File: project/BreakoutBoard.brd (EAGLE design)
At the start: 45.2 x 45.2 mm, 2 parts, among them J1 XF2L-2435-1, X1 LCD

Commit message: Layout complete
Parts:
- added B1: RESET, alps:SKSCLDE010
- added B2: BOOT, alps:SKSCLDE010
- added C1: 22pF/50V, SparkFun-Capacitors:0402-TIGHT
- added C105: 2.2uF/16V, rcl:C0603
- added C106: 4.7uF/16V, rcl:C0603
- added C107: 22pF/50V, rcl:C0402
- added C17: 10uF/16V, rcl:C0603
- added C18: 0.1uF/10V, rcl:C0402
- added C19: 1uF/16V, rcl:C0402
- added C2, C5: 10uF/16V, SparkFun-Capacitors:0603
- added C3, C4: 0.1uF/10V, SparkFun-Capacitors:0402
- added C86: (no value), rcl:C0402
- added CN2: (no value), adafruit:JST-PH-2-SMT
- added D1, D15: (no value), diode:SOD123
- added D10, D8, D9: LESD5D5.0CT1G, discrete:SOD523
- added D11, D12, D2: LESD8D3.3CAT5G, discrete:SOD882
- added D19: (no value), adafruit:SOD-523
- added D3: (no value), led:CHIPLED_1206
- added J2: I2C2, SparkFun-Connectors:JST04_1MM_VERT
- added J3: LCD, ER-CON0.4-24P:OK-24F024-04
- added L1: 2.2μH, SparkFun-Coils:INDUCTOR_4X4MM
- added L6: 10uH_0.8A, discrete:L3012S
- added R1, R13: 10K, rcl:R0402
- added R111, R112: 0, rcl:R0201
- added R12, R123: 0, rcl:R0603
- added R126: 6.6, rcl:R0402
- added R127: 10, rcl:R0402
- added R2: 680K, rcl:R0402
- added R3: 150K, rcl:R0402
- added R74: 51, rcl:R0201
- added TP1, TP2: (no value), SparkFun-Connectors:PAD.03X.03
- added U1: SY8088, discrete:SOT23-5
- added U15: BD60A60NUX, discrete:VSON008X2030
- added U4: ESP32-S3-WROOM-1, espressif:QFN60_ESP32-S3-WROOM-1_EXP
- J1: value XF2L-2435-1 -> I2C1; device con-omron:XF2L-2435-1 -> SparkFun-Connectors:JST04_1MM_VERT
- X1: value LCD -> (none); device ER-CON0.4-24P:OK-24F024-04 -> Adafruit ItsyBitsy nRF52840 Express:MICROBUILDER_4UCONN_20329
- moved X1 21.5 mm to (19.0, 5.00), turned to 0 degrees
- moved J1 18.1 mm to (2.00, 15.5), flipped to the top, turned to 270 degrees
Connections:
- removed net N$10: J1.10, X1.10
- removed net N$11: J1.11, X1.11
- removed net N$12: J1.12, X1.12
- removed net N$13: J1.13, X1.13
- removed net N$14: J1.14, X1.14
- removed net N$15: J1.15, X1.15
- removed net N$16: J1.16, X1.16
- removed net N$17: J1.17, X1.17
- removed net N$18: J1.18, X1.18
- removed net N$19: J1.19, X1.19
- removed net N$20: J1.20, X1.20
- removed net N$21: J1.21, X1.21
- removed net N$22: J1.22, X1.22
- removed net N$23: J1.23, X1.23
- removed net N$24: J1.24, X1.24
- removed net N$3: J1.3, X1.3
- removed net N$5: J1.5, X1.5
- new net ESP_3V3: C17.1, C18.1, D2.C, R12.2, R13.1, U4.2
- new net GND: B1.1, B2.1, C105.2, C106.2, C107.2, C17.2, C18.2, C19.2, C2.2, C3.2, C4.2, C5.2, C86.2, CN2.2, D10.A, D11.A, D12.A, D2.A, D8.A, D9.A, J1.1, J2.1, J3.15, J3.16, J3.3, J3.4, R123.1, R126.1, R3.1, R74.1, TP2.1, U1.2, U15.7, U15.PAD, U4.1, U4.40, U4.41, U4.42, U4.43, U4.44, U4.45, U4.46, U4.47, U4.48, U4.49
- new net GPIO0: B2.3, D12.C, U4.27
- new net GPIO18: J1.4, U4.11
- new net GPIO19: R111.2, U4.13
- new net GPIO20: R112.2, U4.14
- new net GPIO3: J3.21, U4.15
- new net GPIO4: J3.5, U4.4
- new net GPIO40: J2.4, J3.20, U4.33
- new net GPIO41: J2.3, J3.19, U4.34
- new net GPIO45: R127.1, U4.26
- new net GPIO48: J3.10, J3.18, U15.1, U4.25
- new net GPIO5: J3.9, U4.5
- new net GPIO6: J3.8, U4.6
- new net GPIO7: J3.6, U4.7
- new net GPIO8: J1.3, U4.12
- new net LED_A: C105.1, D19.K, J3.23, J3.24, U15.6
- new net LED_DIM: C107.1, R127.2, U15.3
- new net LED_K: J3.1, J3.2, U15.5
- new net MCU_RST: B1.3, C19.1, D11.C, R13.2, U4.3
- new net MCU_VDD: C1.1, C4.1, C5.1, C86.1, D3.A, J1.2, J2.2, J3.11, J3.12, J3.13, J3.14, J3.17, L1.P$2, R12.1, R2.2, TP1.1
- new net USB_5V: C106.1, C2.1, C3.1, D1.C, D15.C, L6.P$1, R1.1, U1.4, U15.2
- new net USB_DN: D9.C, R111.1, X1.D-
- new net USB_DP: D10.C, R112.1, X1.D+
- new net USB_G: R123.2, X1.BASE@1, X1.BASE@2, X1.GND, X1.SPRT@1, X1.SPRT@2, X1.SPRT@3, X1.SPRT@4
- new net USB_VBUS: D1.A, D8.C, X1.VBUS
- net N$1: now also D19.A, L6.P$2, U15.8; no longer J1.1, X1.1
- net N$2: now also D3.C, R74.2; no longer J1.2, X1.2
- net N$4: now also CN2.1, D15.A; no longer J1.4, X1.4
- net N$6: now also R1.2, U1.1; no longer J1.6, X1.6
- net N$7: now also L1.P$1, U1.3; no longer J1.7, X1.7
- net N$8: now also C1.2, R2.1, R3.2, U1.5; no longer J1.8, X1.8
- net N$9: now also R126.2, U15.4; no longer J1.9, X1.9
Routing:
- net MCU_VDD: track 0.00 -> 84.3 mm, vias 0 -> 2
- net GPIO48: track 0.00 -> 56.4 mm, vias 0 -> 2
- net USB_5V: track 0.00 -> 48.7 mm, vias 0 -> 3
- net GPIO40: track 0.00 -> 41.8 mm, vias 0 -> 4
- net GPIO41: track 0.00 -> 40.5 mm, vias 0 -> 3
- net GND: track 0.00 -> 37.8 mm, vias 0 -> 56
- net N$18: track 31.3 -> 0.00 mm, vias 1 -> 0
- net N$17: track 30.8 -> 0.00 mm, vias 1 -> 0
- net N$19: track 30.5 -> 0.00 mm, vias 1 -> 0
- net N$16: track 30.4 -> 0.00 mm, vias 1 -> 0
- net N$20: track 30.1 -> 0.00 mm, vias 1 -> 0
- net N$15: track 30.0 -> 0.00 mm, vias 1 -> 0
- net N$21: track 29.6 -> 0.00 mm, vias 1 -> 0
- net N$14: track 29.6 -> 0.00 mm, vias 1 -> 0
- net N$22: track 29.2 -> 0.00 mm, vias 1 -> 0
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- added copper zone on layer 1, net GND
- added copper zone on layer 16, net GND
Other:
- board size 45.2 x 45.2 mm -> 38 x 38 mm

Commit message: Layout optimization
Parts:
- removed C107: 22pF/50V, rcl:C0402
- removed CN2: (no value), adafruit:JST-PH-2-SMT
- removed R127: 10, rcl:R0402
- removed TP2: (no value), SparkFun-Connectors:PAD.03X.03
- removed X1: (no value), Adafruit ItsyBitsy nRF52840 Express:MICROBUILDER_4UCONN_20329
- added C97: 0.1uF/6.3V, rcl:C0402
- added C98: 4.7uF/6.3V, rcl:C0402
- added J4: I2C1, SparkFun-Connectors:JST04_1MM_VERT
- added J5: I2C2, SparkFun-Connectors:JST04_1MM_VERT
- added U$1, U$2, U$4, U$5: FIDUCIAL, adafruit:FIDUCIAL_1MM
- C1: device SparkFun-Capacitors:0402-TIGHT -> rcl:C0402
- C2: device SparkFun-Capacitors:0603 -> rcl:C0603
- C3: device SparkFun-Capacitors:0402 -> rcl:C0603
- C4: device SparkFun-Capacitors:0402 -> rcl:C0402
- C5: device SparkFun-Capacitors:0603 -> rcl:C0402
- C86: value (none) -> 0.1uF/6.3V
- J1: value I2C1 -> (none); device SparkFun-Connectors:JST04_1MM_VERT -> Adafruit ItsyBitsy nRF52840 Express:MICROBUILDER_4UCONN_20329
- J2: value I2C2 -> (none); device SparkFun-Connectors:JST04_1MM_VERT -> adafruit:JST-PH-2-SMT
- R126: value 6.6 -> 20K
- TP1: value (none) -> TPTP06R; device SparkFun-Connectors:PAD.03X.03 -> testpad:TP06R
- moved J2 31.2 mm to (33.0, 19.0), turned to 90 degrees
- moved TP1 22.0 mm to (30.6, 30.7)
- moved J1 20.0 mm to (19.0, 5.00), turned to 0 degrees
- moved R2 8.55 mm to (19.5, 9.60), turned to 180 degrees
- moved C1 8.50 mm to (19.5, 10.5), flipped to the bottom, turned to 0 degrees
- moved D12 6.93 mm to (33.4, 9.40)
- moved R3 5.56 mm to (19.5, 8.60), turned to 0 degrees
- moved R74 4.10 mm to (9.39, 9.15), turned to 180 degrees
- moved R126 3.49 mm to (29.2, 30.6), flipped to the bottom
- moved D19 2.24 mm to (33.0, 28.0), turned to 0 degrees
- moved L6 2.00 mm to (33.0, 25.0), flipped to the bottom, turned to 270 degrees
- moved C105 1.77 mm to (30.5, 30.5), turned to 270 degrees
- moved C4 1.70 mm to (29.2, 11.0), turned to 45 degrees
- moved C5 1.31 mm to (30.5, 10.2), turned to 45 degrees
- moved D2 1.30 mm to (7.90, 31.0)
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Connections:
- removed net LED_DIM: C107.1, R127.2, U15.3
- net GND: now also B1.2, B2.2, C97.2, C98.2, J2.2, J4.1, J5.1; no longer C107.2, CN2.2, J1.1, J2.1, TP2.1
- net GPIO0: now also B2.4
- net GPIO18: now also J4.4; no longer J1.4
- net GPIO40: now also J5.4; no longer J2.4
- net GPIO41: now also J5.3; no longer J2.3
- net GPIO45: now also U15.3; no longer R127.1
- net GPIO8: now also J4.3; no longer J1.3
- net LED_K: now also TP1.TP
- net MCU_RST: now also B1.4
- net MCU_VDD: now also C97.1, C98.1, J4.2, J5.2, U15.2; no longer J1.2, J2.2, TP1.1
- net N$4: now also J2.1; no longer CN2.1
- net USB_5V: no longer U15.2
- net USB_DN: now also J1.D-; no longer X1.D-
- net USB_DP: now also J1.D+; no longer X1.D+
- net USB_G: now also J1.BASE@1, J1.BASE@2, J1.GND, J1.SPRT@1, J1.SPRT@2, J1.SPRT@3, J1.SPRT@4; no longer X1.BASE@1, X1.BASE@2, X1.GND, X1.SPRT@1, X1.SPRT@2, X1.SPRT@3, X1.SPRT@4
- net USB_VBUS: now also J1.VBUS; no longer X1.VBUS
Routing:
- net GPIO48: track 56.4 -> 37.1 mm
- net MCU_VDD: track 84.3 -> 99.7 mm, vias 2 -> 5
- net GPIO0: track 20.9 -> 11.6 mm
- net N$8: track 12.4 -> 4.06 mm, vias 2 -> 1
- net GND: track 37.8 -> 46.1 mm, vias 56 -> 60
- net GPIO45: track 14.7 -> 21.5 mm, vias 0 -> 1
- net LED_DIM: track 4.68 -> 0.00 mm, vias 1 -> 0
- net LED_A: track 14.5 -> 17.7 mm, vias 1 -> 2
- net USB_5V: track 48.7 -> 45.6 mm
- net GPIO7: track 14.1 -> 11.1 mm
- net LED_K: track 12.9 -> 15.7 mm
- net N$6: track 2.24 -> 4.63 mm, vias 1 -> 0
- net GPIO6: track 12.3 -> 9.94 mm
- net GPIO5: track 10.7 -> 8.81 mm
- net N$1: track 3.79 -> 5.25 mm
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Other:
- board text added: "5V"
- board text added: "BOOT"
- board text added: "I2C"
- board text added: "RST"

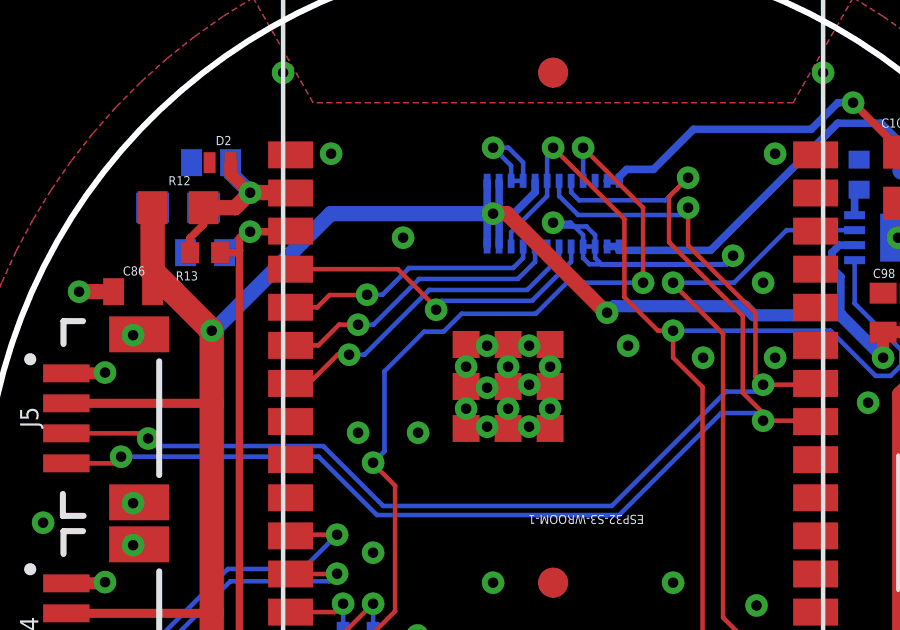
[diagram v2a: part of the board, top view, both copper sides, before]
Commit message: Display pinout fix
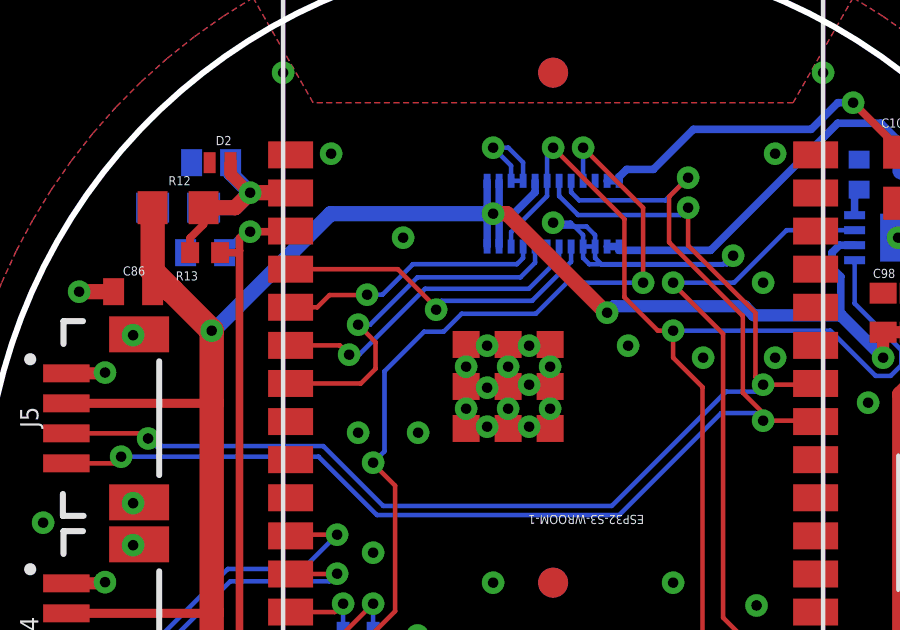
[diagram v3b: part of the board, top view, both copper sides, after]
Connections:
- net GPIO6: now also J3.6; no longer J3.8
- net GPIO7: now also J3.8; no longer J3.6
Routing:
- net GPIO7: track 11.1 -> 12.0 mm
- net GPIO6: track 9.94 -> 10.8 mm
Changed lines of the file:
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@@
 <drawing>
 <settings>
-<setting alwaysvectorfont="no"/>
+<setting alwaysvectorfont="yes"/>
 <setting verticaltext="up"/>
 </settings>
-<grid distance="1" unitdist="mm" unit="mm" style="lines" multiple="1" display="no" altdistance="0.1" altunitdist="mm" altunit="mm"/>
+<grid distance="50" unitdist="mil" unit="mil" style="lines" multiple="1" display="no" altdistance="5" altunitdist="mil" altunit="mil"/>
 <layers>
 <layer number="1" name="Top" color="4" fill="1" visible="yes" active="yes"/>
@@
 <wire x1="12.7878" y1="26.5878" x2="12.8" y2="26.6" width="0.1524" layer="1"/>
 <wire x1="18" y1="28.205" x2="18" y2="27.824" width="0.1524" layer="16"/>
-<wire x1="18" y1="27.824" x2="17.665" y2="27.489" width="0.1524" layer="16"/>
-<wire x1="17.665" y1="27.489" x2="14.197" y2="27.489" width="0.1524" layer="16"/>
-<wire x1="14.197" y1="27.489" x2="13.308" y2="26.6" width="0.1524" layer="16"/>
+<wire x1="18" y1="27.824" x2="17.792" y2="27.616" width="0.1524" layer="16"/>
+<wire x1="17.792" y1="27.616" x2="14.324" y2="27.616" width="0.1524" layer="16"/>
+<wire x1="14.324" y1="27.616" x2="13.308" y2="26.6" width="0.1524" layer="16"/>
 <wire x1="13.308" y1="26.6" x2="12.8" y2="26.6" width="0.1524" layer="16"/>
 </signal>
 <signal name="GPIO6">
 <contactref element="U4" pad="6"/>
-<via x="12.5" y="25.6" extent="1-16" drill="0.35"/>
-<wire x1="10.25" y1="24.91" x2="10.34" y2="25" width="0.1524" layer="1"/>
-<contactref element="J3" pad="8"/>
-<wire x1="10.25" y1="24.91" x2="11.175" y2="24.91" width="0.1524" layer="1"/>
-<wire x1="11.865" y1="25.6" x2="12.5" y2="25.6" width="0.1524" layer="1"/>
-<wire x1="11.865" y1="25.6" x2="11.175" y2="24.91" width="0.1524" layer="1"/>
-<wire x1="18.4" y1="28.205" x2="18.4" y2="27.697" width="0.1524" layer="16"/>
-<wire x1="18.4" y1="27.697" x2="17.827" y2="27.124" width="0.1524" layer="16"/>
-<wire x1="17.827" y1="27.124" x2="14.532" y2="27.124" width="0.1524" layer="16"/>
-<wire x1="14.532" y1="27.124" x2="13.008" y2="25.6" width="0.1524" layer="16"/>
-<wire x1="13.008" y1="25.6" x2="12.5" y2="25.6" width="0.1524" layer="16"/>
+<via x="12.2" y="24.6" extent="1-16" drill="0.35"/>
+<contactref element="J3" pad="6"/>
+<wire x1="12.2" y1="24.6" x2="12.535" y2="24.6" width="0.1524" layer="16"/>
+<wire x1="18.1922875" y1="26.797" x2="19.2" y2="27.8047125" width="0.1524" layer="16"/>
+<wire x1="19.2" y1="27.8047125" x2="19.2" y2="28.205" width="0.1524" layer="16"/>
+<wire x1="12.535" y1="24.6" x2="14.732" y2="26.797" width="0.1524" layer="16"/>
+<wire x1="14.732" y1="26.797" x2="18.1922875" y2="26.797" width="0.1524" layer="16"/>
+<wire x1="12.2" y1="24.6" x2="11.89" y2="24.91" width="0.1524" layer="1"/>
+<wire x1="11.89" y1="24.91" x2="10.25" y2="24.91" width="0.1524" layer="1"/>
 </signal>
 <signal name="GPIO7">
 <contactref element="U4" pad="7"/>
-<via x="12.2" y="24.6" extent="1-16" drill="0.35"/>
-<contactref element="J3" pad="6"/>
-<wire x1="10.25" y1="23.64" x2="10.859" y2="23.64" width="0.1524" layer="1"/>
-<wire x1="11.819" y1="24.6" x2="12.2" y2="24.6" width="0.1524" layer="1"/>
-<wire x1="11.819" y1="24.6" x2="10.859" y2="23.64" width="0.1524" layer="1"/>
-<wire x1="18.135" y1="26.759" x2="14.867" y2="26.759" width="0.1524" layer="16"/>
-<wire x1="14.867" y1="26.759" x2="12.708" y2="24.6" width="0.1524" layer="16"/>
-<wire x1="12.708" y1="24.6" x2="12.2" y2="24.6" width="0.1524" layer="16"/>
-<wire x1="19.2" y1="28.205" x2="19.2" y2="27.824" width="0.1524" layer="16"/>
-<wire x1="19.2" y1="27.824" x2="18.135" y2="26.759" width="0.1524" layer="16"/>
+<via x="12.5" y="25.6" extent="1-16" drill="0.35"/>
+<contactref element="J3" pad="8"/>
+<wire x1="10.25" y1="23.64" x2="12.591" y2="23.64" width="0.1524" layer="1"/>
+<wire x1="13.081" y1="24.13" x2="13.081" y2="25.019" width="0.1524" layer="1"/>
+<wire x1="13.081" y1="25.019" x2="12.5" y2="25.6" width="0.1524" layer="1"/>
+<wire x1="12.591" y1="23.64" x2="13.081" y2="24.13" width="0.1524" layer="1"/>
+<wire x1="12.5" y1="25.6" x2="12.9" y2="25.6" width="0.1524" layer="16"/>
+<wire x1="12.9" y1="25.6" x2="14.478" y2="27.178" width="0.1524" layer="16"/>
+<wire x1="17.91205625" y1="27.178" x2="18.4" y2="27.66594375" width="0.1524" layer="16"/>
+<wire x1="18.4" y1="27.66594375" x2="18.4" y2="28.205" width="0.1524" layer="16"/>
+<wire x1="14.478" y1="27.178" x2="17.91205625" y2="27.178" width="0.1524" layer="16"/>
 </signal>
 <signal name="GPIO48">
@@
 <wire x1="17" y1="29.3" x2="17.46" y2="29.3" width="0.508" layer="1"/>
 <via x="20.8" y="26" extent="1-16" drill="0.35"/>
-<wire x1="20.8" y1="26" x2="20.75" y2="26.145" width="0.3048" layer="16"/>
 <contactref element="U15" pad="2"/>
 <wire x1="25.69135" y1="25.9106" x2="25.38655" y2="26.2154" width="0.4064" layer="16"/>
